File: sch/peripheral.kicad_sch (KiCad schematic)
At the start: 3 parts, among them J3 USB_A

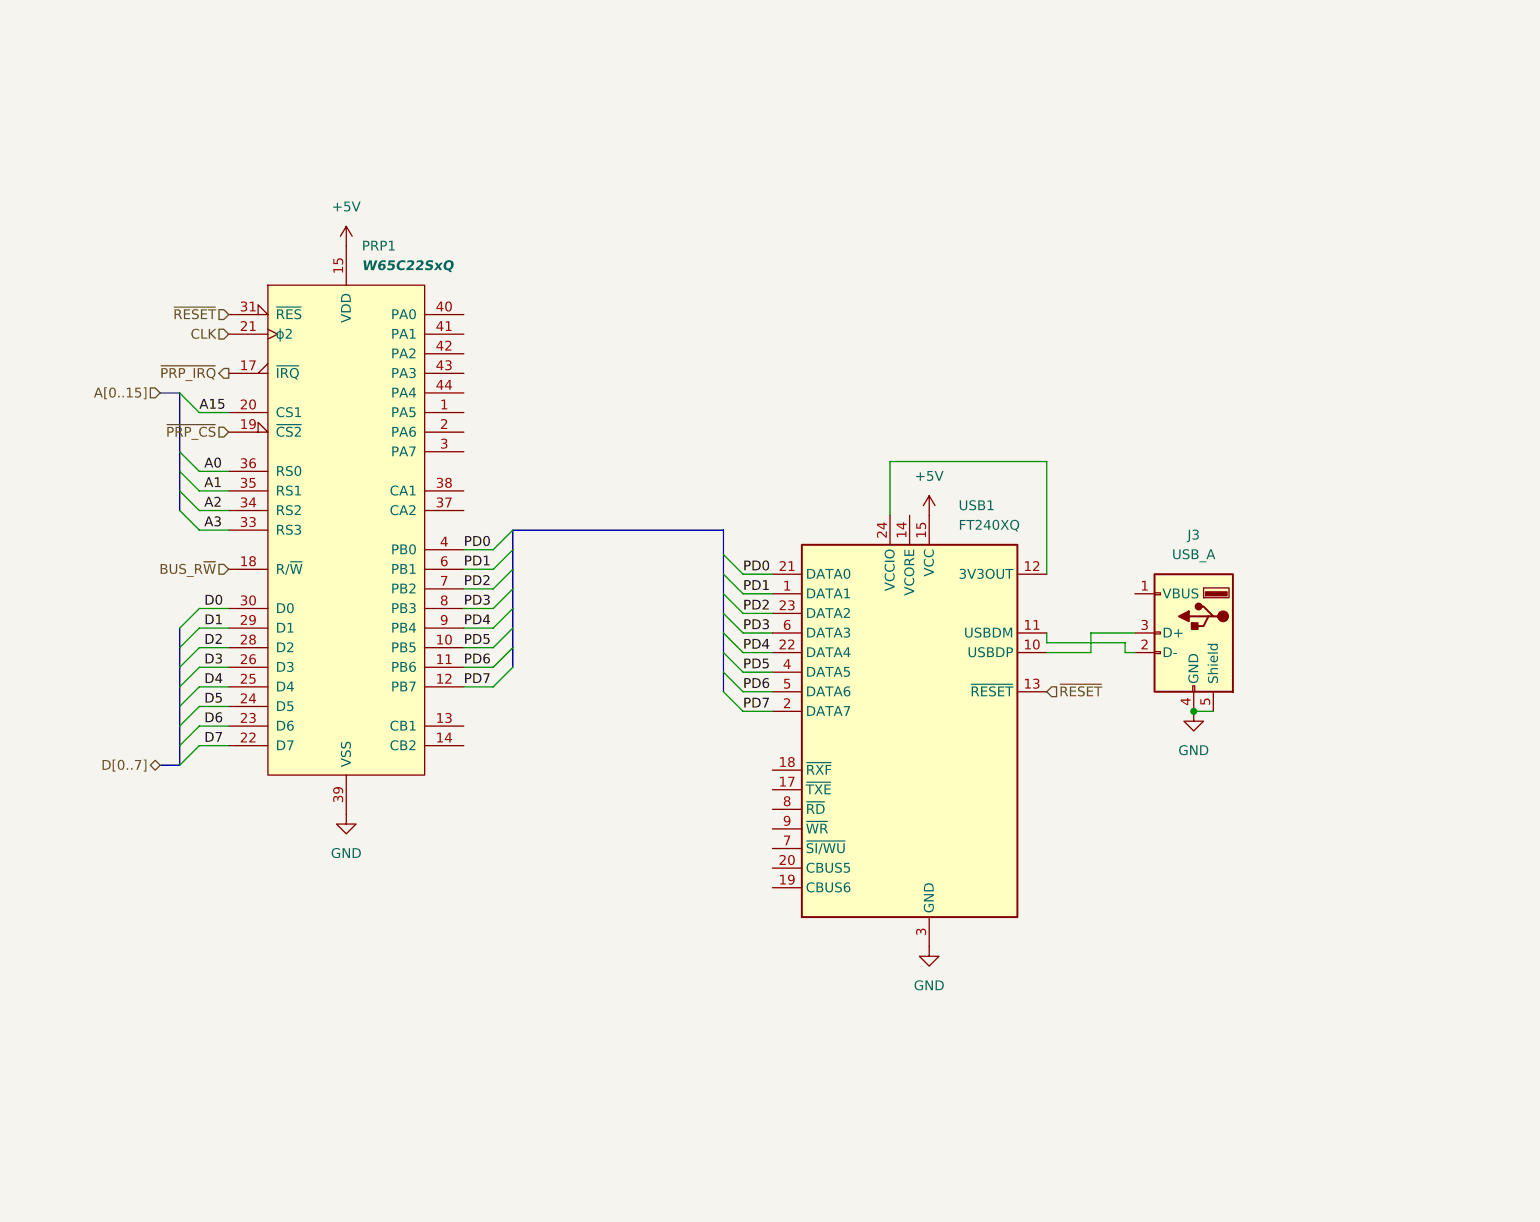
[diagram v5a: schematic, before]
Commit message: Serial, debug and prph headers
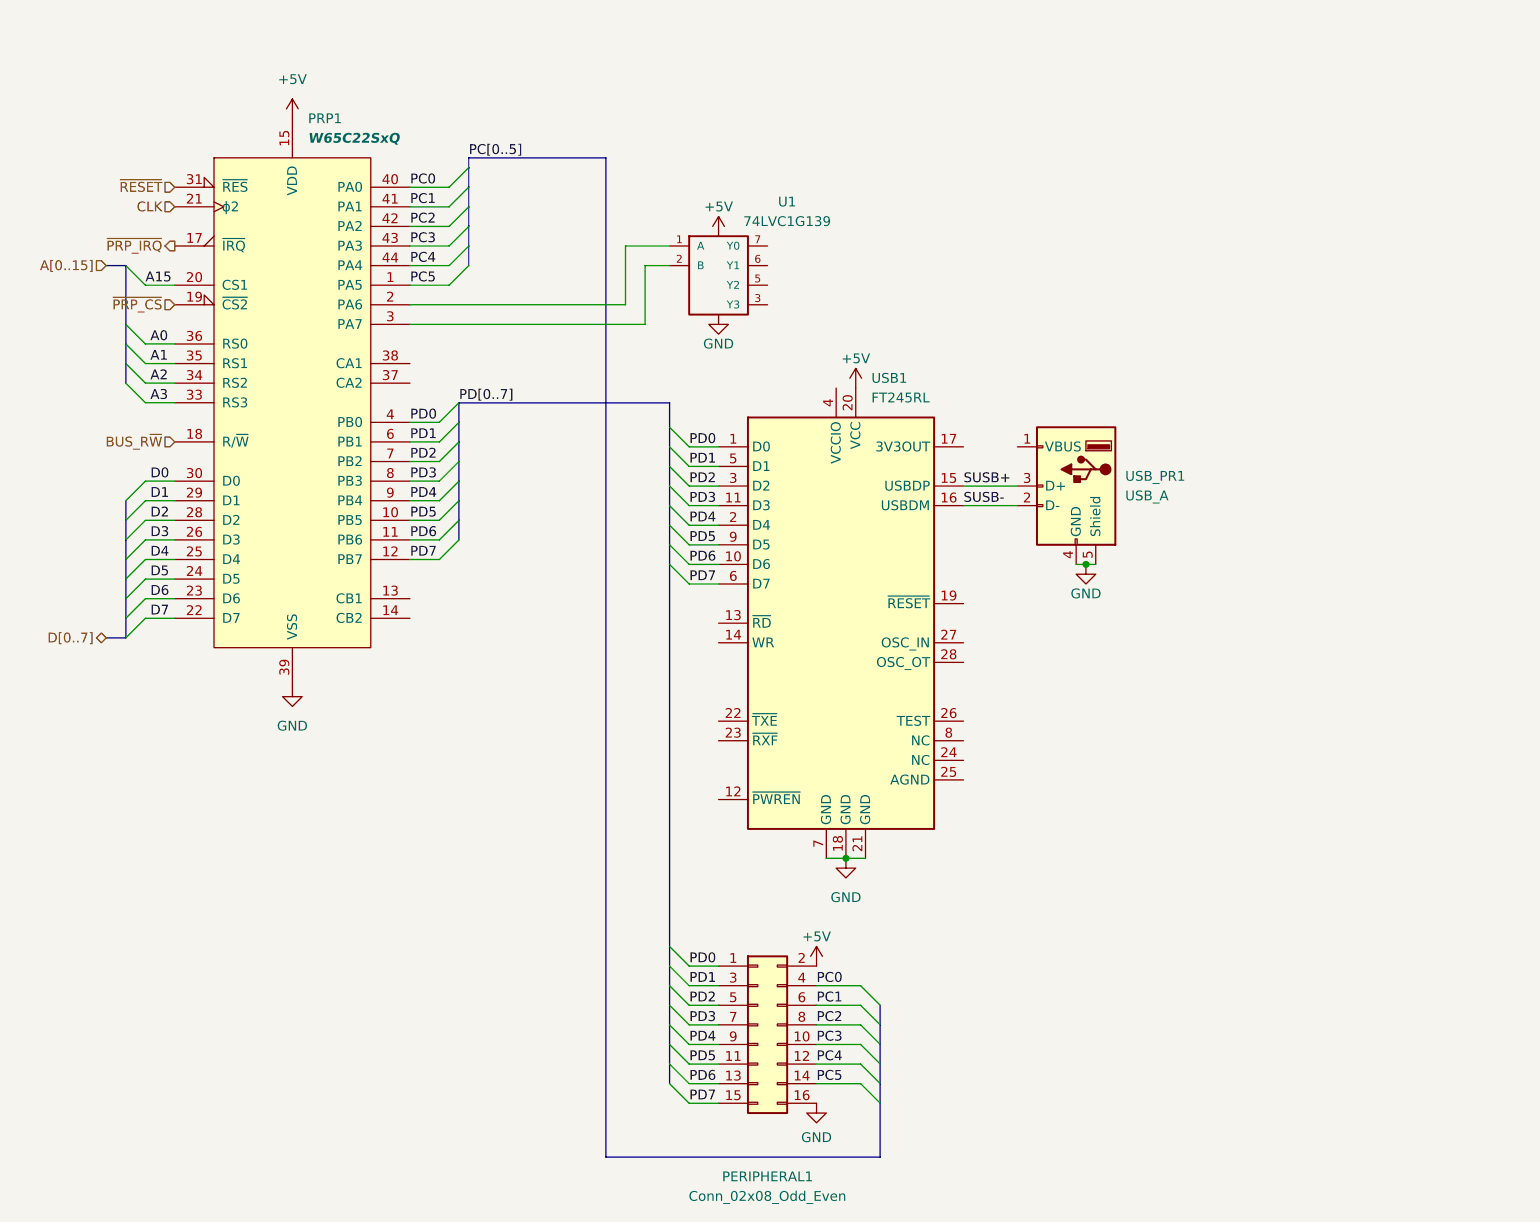
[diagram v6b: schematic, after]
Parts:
- removed USB1: FT240XQ, Package_DFN_QFN:QFN-24-1EP_4x4mm_P0.5mm_EP2.6x2.6mm, symbol Interface_USB:FT240XQ
- added PERIPHERAL1: Conn_02x08_Odd_Even, Connector_PinHeader_2.00mm:PinHeader_2x08_P2.00mm_Vertical, symbol Connector_Generic:Conn_02x08_Odd_Even
- added U1: 74LVC1G139, symbol 74xGxx:74LVC1G139
- added USB1: FT245RL, Package_SO:SSOP-28_5.3x10.2mm_P0.65mm, symbol Custom:FT245RL
- renumbered J3 to USB_PR1
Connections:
- net +5V: now also PERIPHERAL1.2 (Pin_2), U1.8 (VCC), USB1.20 (VCC)
- net GND: now also PERIPHERAL1.16 (Pin_16), U1.4 (GND), USB1.18 (GND), USB1.21 (GND), USB1.7 (GND)
- net PD0: now also PERIPHERAL1.1 (Pin_1), USB1.1 (D0)
- net PD1: now also PERIPHERAL1.3 (Pin_3), USB1.5 (D1)
- net PD2: now also PERIPHERAL1.5 (Pin_5), USB1.3 (D2)
- net PD3: now also PERIPHERAL1.7 (Pin_7), USB1.11 (D3)
- net PD4: now also PERIPHERAL1.9 (Pin_9), USB1.2 (D4)
- net PD5: now also PERIPHERAL1.11 (Pin_11), USB1.9 (D5)
- net PD6: now also PERIPHERAL1.13 (Pin_13), USB1.10 (D6)
- net PD7: now also PERIPHERAL1.15 (Pin_15), USB1.6 (D7)
- net SUSB+: now reaches USB_PR1.3 (D+)
- net SUSB+: now also USB1.15 (USBDP)
- net SUSB-: now reaches USB_PR1.2 (D-)
- net SUSB-: now also USB1.16 (USBDM)
- net PC5: now reaches PRP1.1 (PA5)
- net PC5: now also PERIPHERAL1.14 (Pin_14)
- net at PRP1.2 (PA6): now also U1.1 (A)
- net at PRP1.3 (PA7): now also U1.2 (B)
- net PC0: now reaches PRP1.40 (PA0)
- net PC0: now also PERIPHERAL1.4 (Pin_4)
- net PC1: now reaches PRP1.41 (PA1)
- net PC1: now also PERIPHERAL1.6 (Pin_6)
- net PC2: now reaches PRP1.42 (PA2)
- net PC2: now also PERIPHERAL1.8 (Pin_8)
- net PC3: now reaches PRP1.43 (PA3)
- net PC3: now also PERIPHERAL1.10 (Pin_10)
- net PC4: now reaches PRP1.44 (PA4)
- net PC4: now also PERIPHERAL1.12 (Pin_12)
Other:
- moved on the sheet: PRP1, USB_PR1

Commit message: First completed routing
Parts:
- added C21, C22: (no value), symbol Device:C_Small
- renumbered USB_PR1 to USB_P1
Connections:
- net +5V: now also USB1.4 (VCCIO), C21.1, C22.1
- net GND: now also USB1.25 (AGND), C21.2, C22.2
- net PC0: now also USB1.13 (~{RD})
- net PC1: now also USB1.14 (WR)
- net PC2: now also USB1.22 (~{TXE})
- net PC3: now also USB1.23 (~{RXF})
- net PC4: now also USB1.12 (~{PWREN})
- net ~{RESET}: now also USB1.19 (~{RESET})
- net at USB1.17 (3V3OUT): now also USB_P1.1 (VBUS)
- no-connect marks 0 -> 5
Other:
- moved on the sheet: PERIPHERAL1, U1, USB1, USB_P1

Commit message: Gerber Plots
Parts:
- C21, C22: value (none) -> 100nF; footprint (none) -> Capacitor_SMD:C_0805_2012Metric
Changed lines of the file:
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@@
       (effects (font (size 1.27 1.27)) (justify left))
     )
-    (property "Value" "" (id 1) (at 42.545 29.845 0)
+    (property "Value" "100nF" (id 1) (at 42.545 29.845 0)
       (effects (font (size 1.27 1.27)) (justify left))
     )
-    (property "Footprint" "" (id 2) (at 50.8 28.575 0)
+    (property "Footprint" "Capacitor_SMD:C_0805_2012Metric" (id 2) (at 50.8 28.575 0)
       (effects (font (size 1.27 1.27)) hide)
     )
@@
       (effects (font (size 1.27 1.27)) hide)
     )
-    (property "Value" "" (id 1) (at 117.475 65.405 0))
+    (property "Value" "GND" (id 1) (at 117.475 65.405 0))
     (property "Footprint" "" (id 2) (at 120.65 63.5 0)
       (effects (font (size 1.27 1.27)) hide)
@@
       (effects (font (size 1.27 1.27)) hide)
     )
-    (property "Value" "" (id 1) (at 50.8 35.56 0))
+    (property "Value" "GND" (id 1) (at 50.8 35.56 0))
     (property "Footprint" "" (id 2) (at 50.8 31.115 0)
       (effects (font (size 1.27 1.27)) hide)
@@
       (effects (font (size 1.27 1.27)) (justify left))
     )
-    (property "Value" "" (id 1) (at 123.825 62.2362 0)
+    (property "Value" "100nF" (id 1) (at 123.825 62.2362 0)
       (effects (font (size 1.27 1.27)) (justify left))
     )
-    (property "Footprint" "" (id 2) (at 120.65 60.96 0)
+    (property "Footprint" "Capacitor_SMD:C_0805_2012Metric" (id 2) (at 120.65 60.96 0)
       (effects (font (size 1.27 1.27)) hide)
     )
